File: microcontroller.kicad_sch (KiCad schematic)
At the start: 51 parts, among them SW1 SW_SPST, SW2 SW_SPST, U2 W25Q16JVSS, U3 RP2040, U4 W25Q16JVSS, Y1 12MHz/10pF, Y2 12MHz/10pF

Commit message: refac: reannotates designators
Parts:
- renumbered C27 to C10, C12 to C11, C14 to C12, C15 to C14, C1 to C15, C9 to C16, C2 to C17, C8 to C18, C3 to C19, C7 to C20, C16 to C21, C19 to C22, C20 to C23, C21 to C24, C22 to C25, C23 to C26, C24 to C27, C25 to C28, C18 to C29, C26 to C30, C17 to C31, C4 to C32, C5 to C33, C6 to C34, C29 to C35, C28 to C36, C30 to C37, C31 to C38, C32 to C39, C33 to C40, C10 to C8, C11 to C9, R1 to R10, R3 to R11, R5 to R12, R6 to R13, R7 to R14, R8 to R15, R4 to R16, R9 to R17, R10 to R18, R2 to R9, U4 to U3, U2 to U4, U1 to U5, U3 to U6

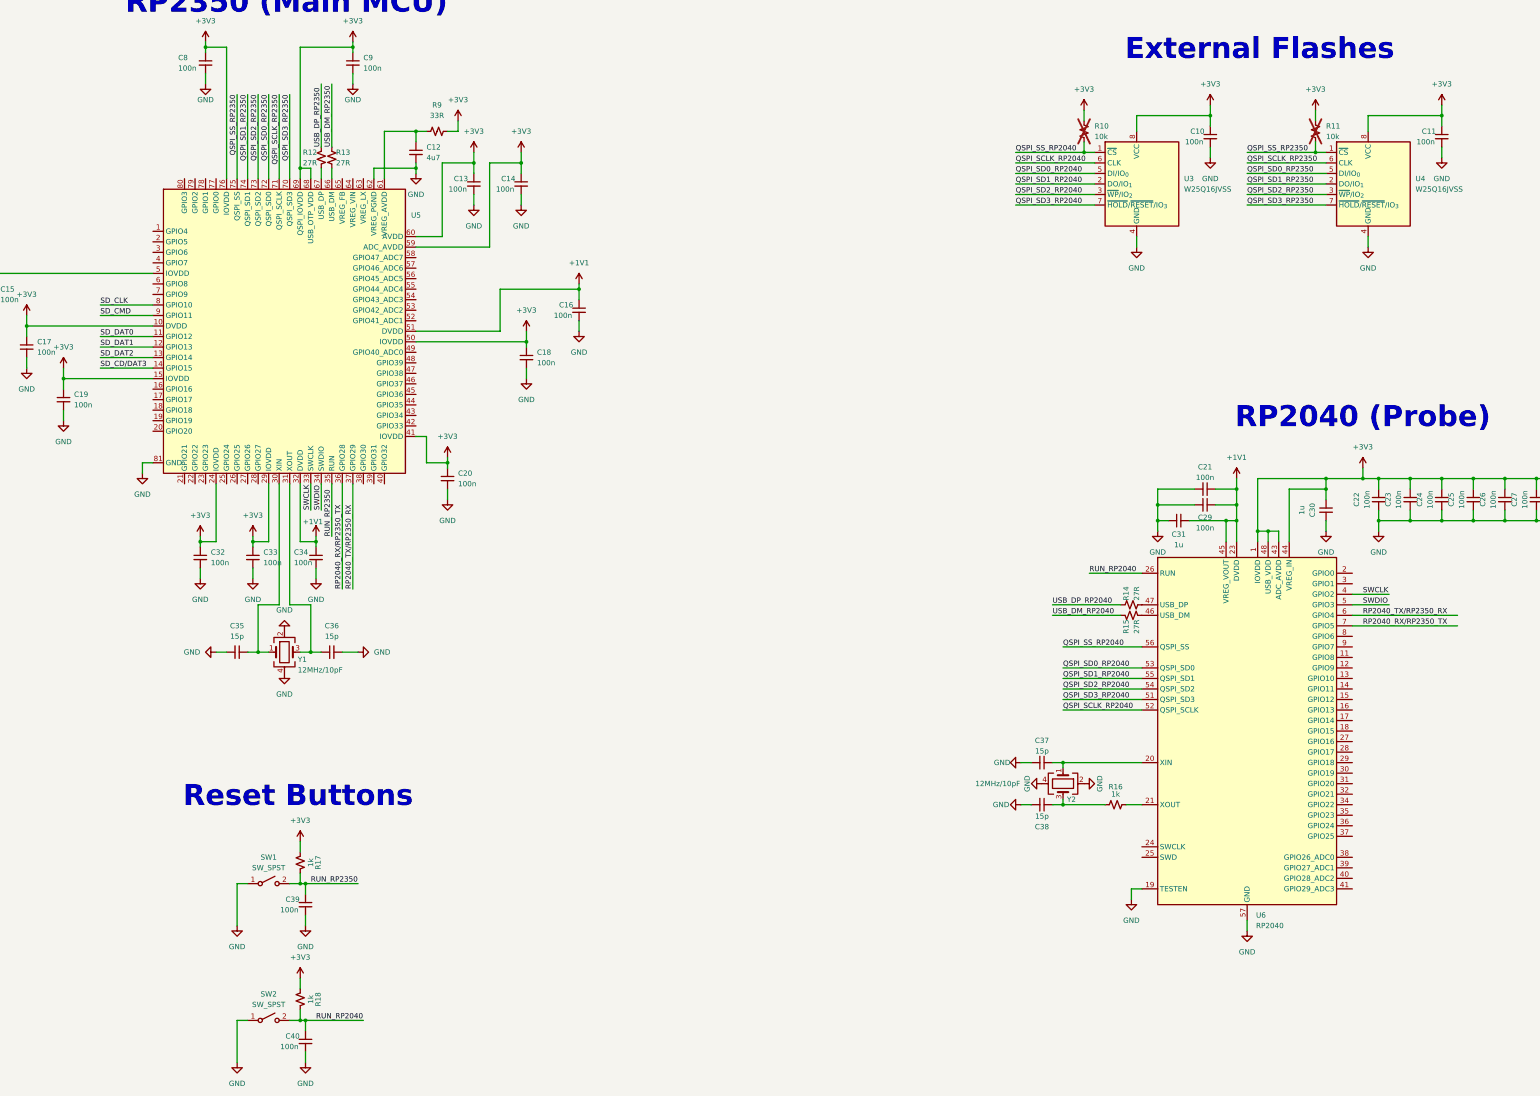
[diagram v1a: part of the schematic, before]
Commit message: chore: links global labels
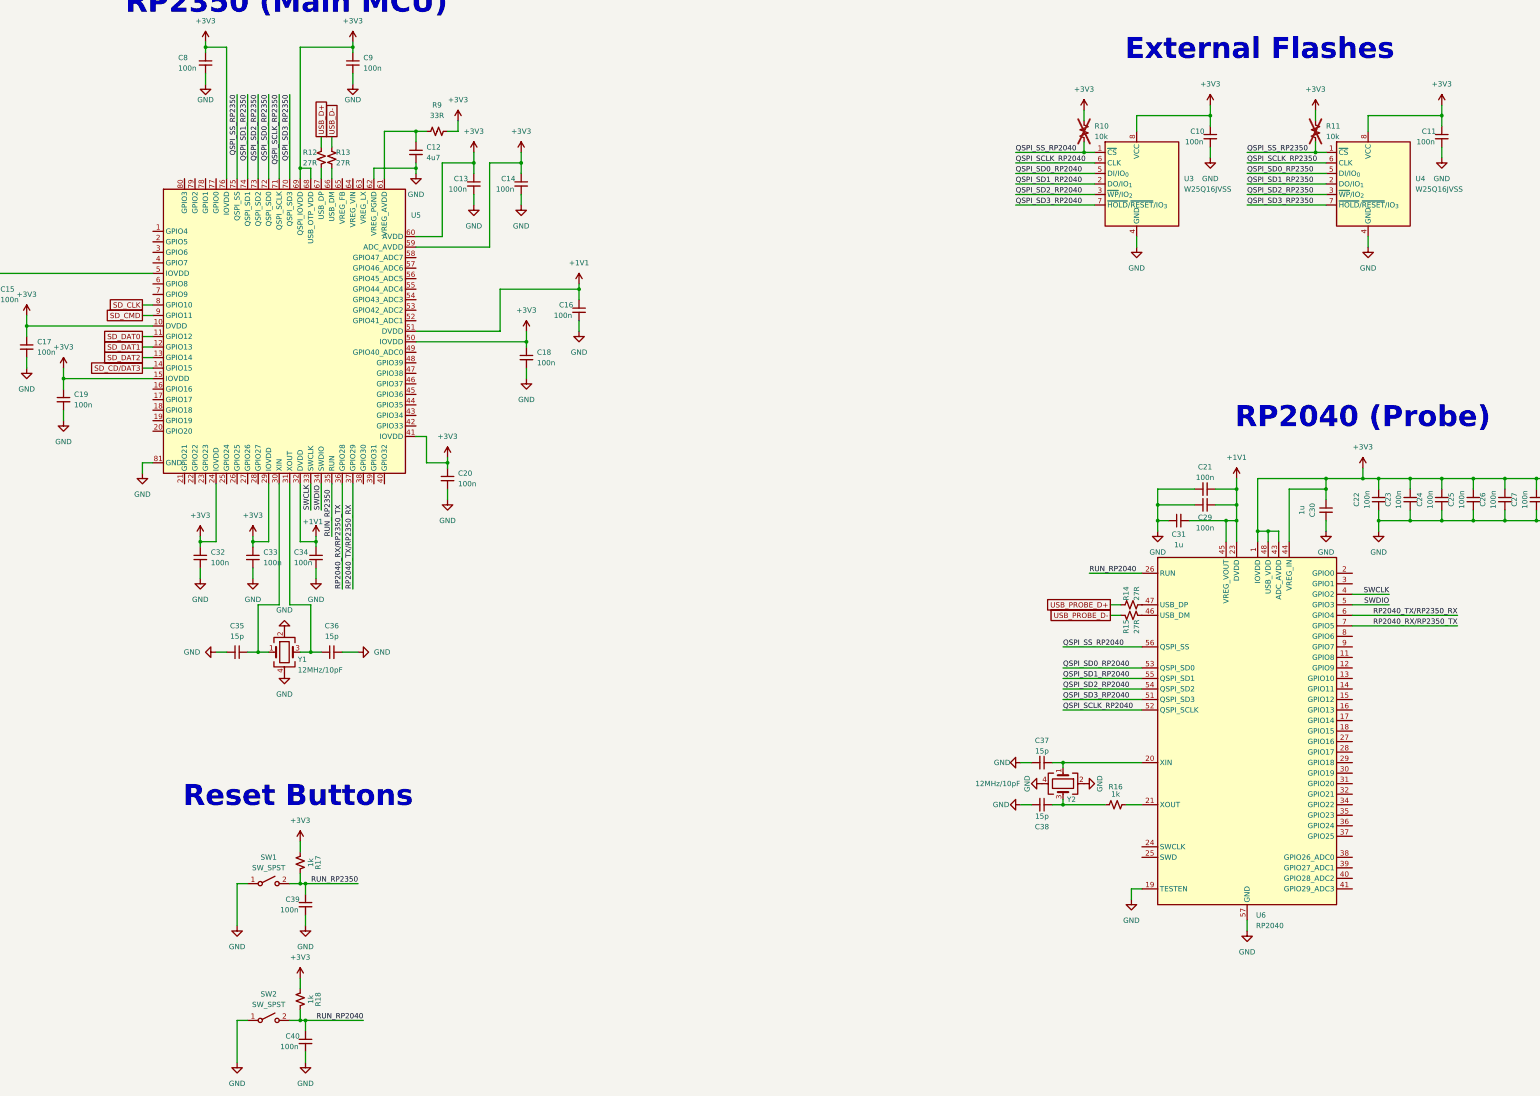
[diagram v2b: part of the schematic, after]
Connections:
- net USB_DM_RP2040 renamed USB_PROBE_D-
- net USB_DM_RP2350 renamed USB_D-
- net USB_DP_RP2040 renamed USB_PROBE_D+
- net USB_DP_RP2350 renamed USB_D+

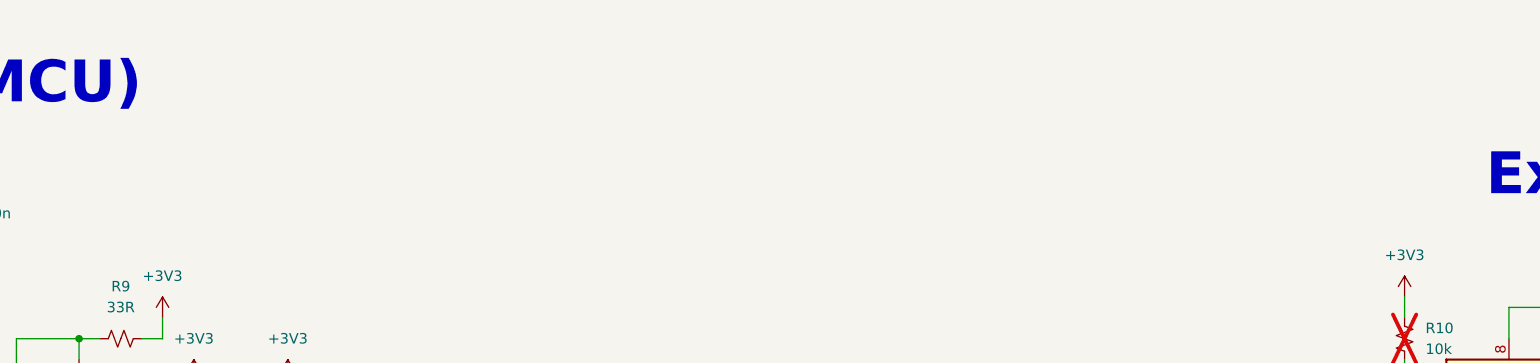
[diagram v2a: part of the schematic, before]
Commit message: chore: adds titles to sheets and organizes root
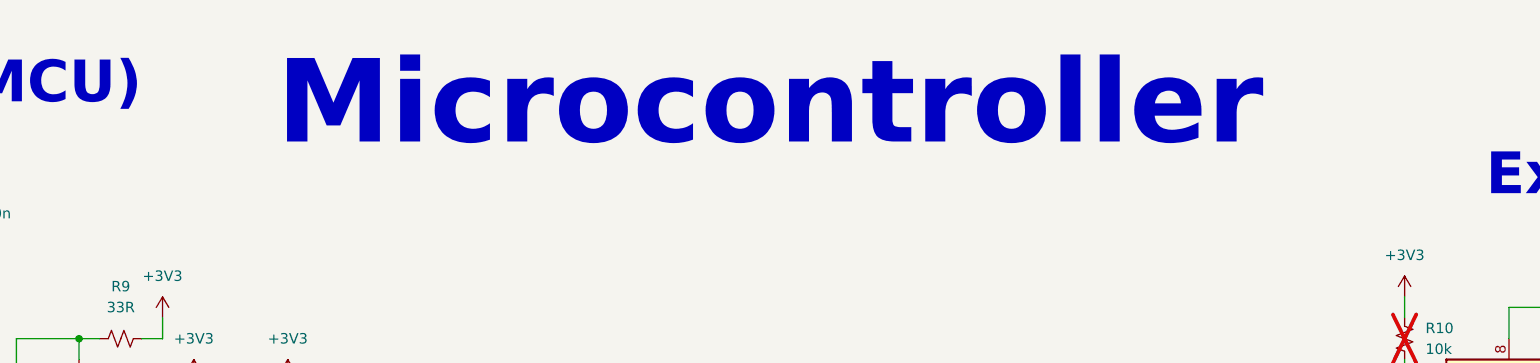
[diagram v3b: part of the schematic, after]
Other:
- note added: "Microcontroller"
- company: (none) -> Os Circuitados
- title: (none) -> Microcontroller
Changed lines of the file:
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@@
 	(generator_version "9.0")
 	(paper "A3")
+	(title_block
+		(title "Microcontroller")
+		(company "Os Circuitados")
+	)
+	(text "Microcontroller"
+		(exclude_from_sim no)
+		(at 209.804 24.892 0)
+		(effects
+			(font
+				(size 10.16 10.16)
+				(thickness 2.032)
+				(bold yes)
+			)
+		)
+	)
 	(text "External Flashes\n"
 		(exclude_from_sim no)

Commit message: refac: standardizes schematic sectorization
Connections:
- net SWCLK_RP2040: now reaches U6.24 (SWCLK)
- net SWDIO_RP2040: now reaches U6.25 (SWD)
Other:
- note added: "Probe Flash/MCU Flash"
- note added: "RESET Buttons"
- note removed: "External Flashes"
- note removed: "Reset Buttons"
- moved on the sheet: C10, C11, C12, C13, C14, C15, C16, C17, C18, C19, C20, C21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

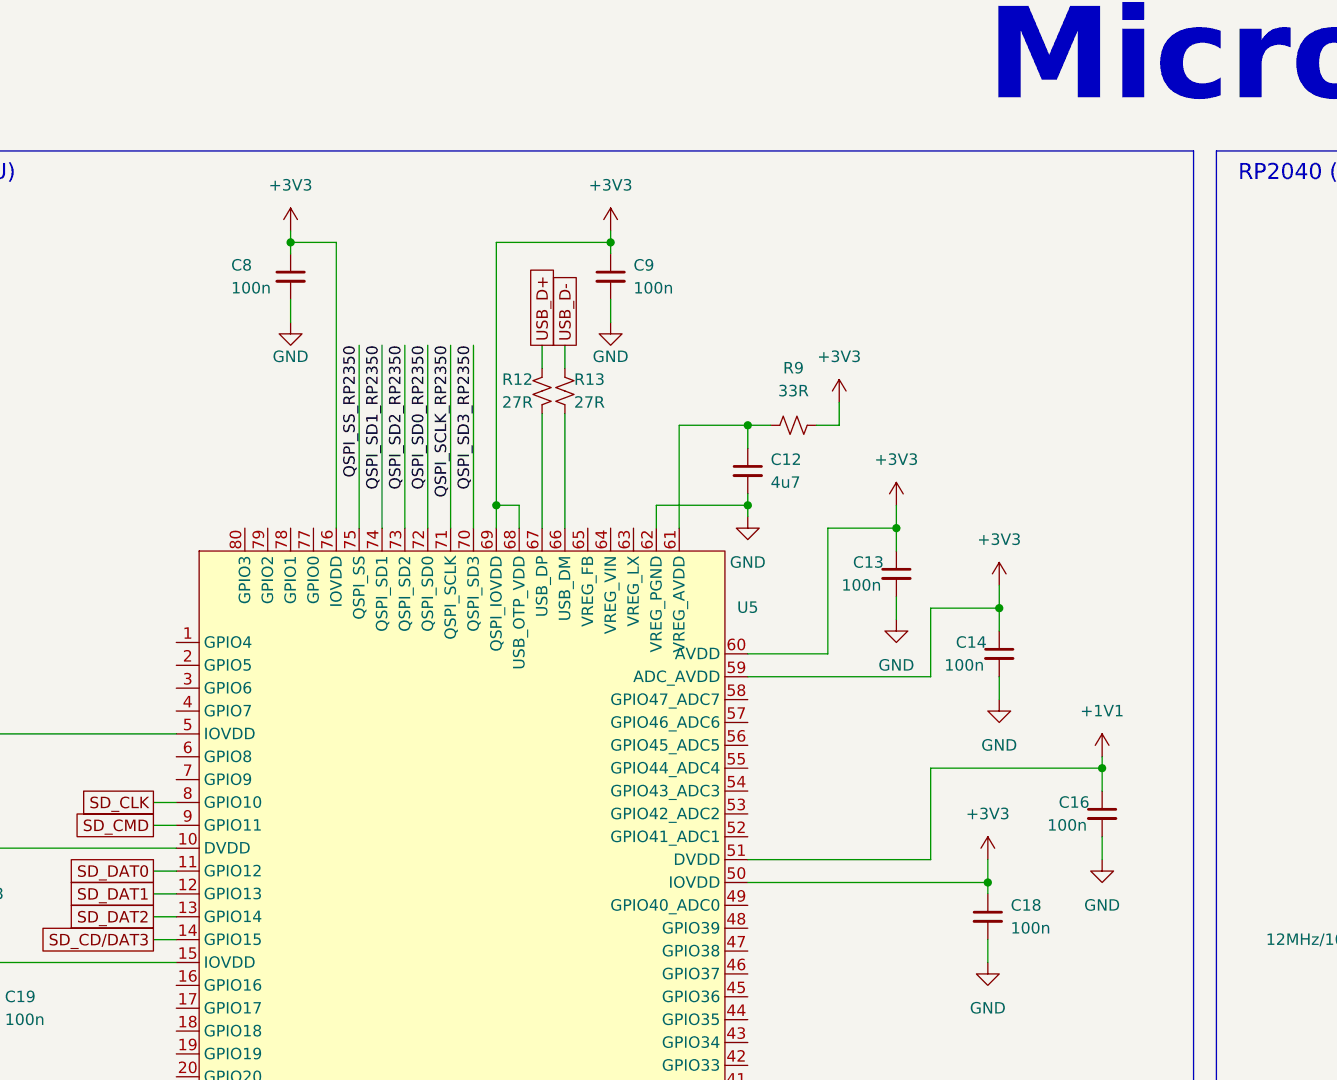
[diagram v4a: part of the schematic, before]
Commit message: feat: adds Vreg circuitry
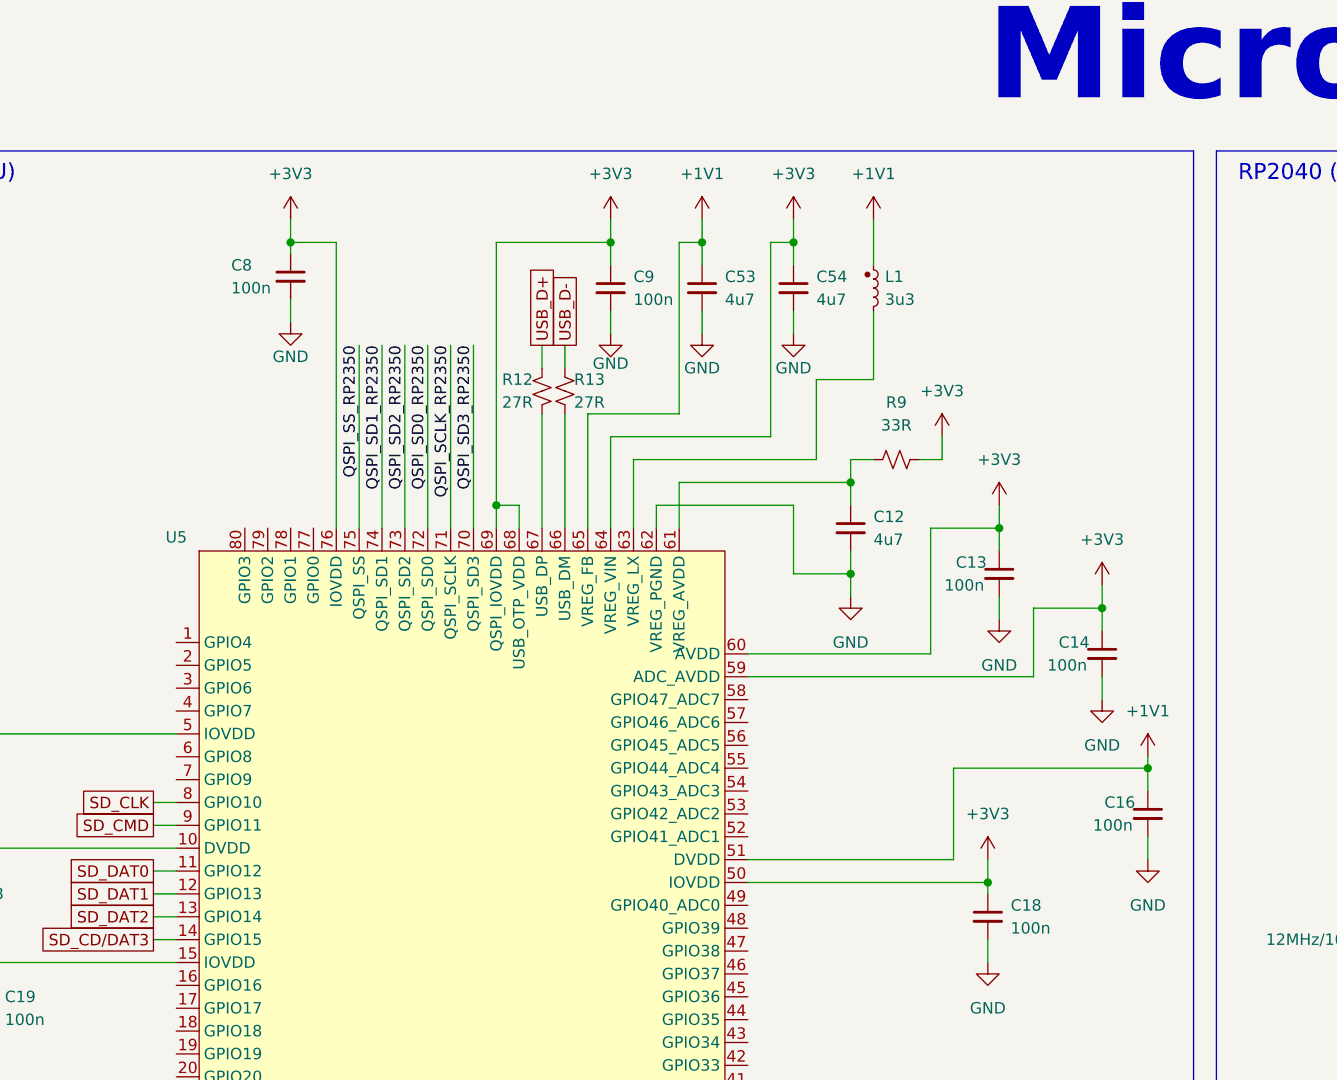
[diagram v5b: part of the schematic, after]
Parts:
- added C53, C54: 4u7, Capacitor_SMD:C_0402_1005Metric, symbol Device:C_Small
- added L1: 3u3, symbol Device:L_Small
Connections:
- net +1V1: now also U5.65 (VREG_FB), C53.1, L1.1
- net +3V3: now also U5.64 (VREG_VIN), C54.1
- net GND: now also C53.2, C54.2
- net at U5.63 (VREG_LX): now also L1.2
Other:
- moved on the sheet: C12, C13, C14, C16, C9, R9

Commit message: feat: adds footprints to Microcontroller sheet circuits
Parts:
- SW1, SW2: footprint (none) -> microcontroller:SMD Button
- U5: footprint (none) -> microcontroller:QFN-80_EP_14x14_Pitch0.4mm
- Y1, Y2: footprint (none) -> microcontroller:XTAL_ABM8-272-T3
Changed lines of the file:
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@@
 			)
 		)
-		(property "Footprint" ""
+		(property "Footprint" "microcontroller:QFN-80_EP_14x14_Pitch0.4mm"
 			(at 91.44 110.49 0)
 			(effects
@@
 			)
 		)
-		(property "Footprint" ""
+		(property "Footprint" "microcontroller:SMD Button"
 			(at 361.95 88.9 0)
 			(effects
@@
 			)
 		)
-		(property "Footprint" ""
+		(property "Footprint" "microcontroller:XTAL_ABM8-272-T3"
 			(at 201.93 119.38 0)
 			(effects
@@
 			)
 		)
-		(property "Footprint" ""
+		(property "Footprint" "microcontroller:SMD Button"
 			(at 361.95 55.88 0)
 			(effects
@@
 			)
 		)
-		(property "Footprint" ""
+		(property "Footprint" "microcontroller:XTAL_ABM8-272-T3"
 			(at 91.44 187.96 0)
 			(effects
